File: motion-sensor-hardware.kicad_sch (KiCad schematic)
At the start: 34 parts, among them J1 MX128-2.54-04P-GN01-Cu-Y-A, J2 MX128-2.54-02P-GN01-Cu-Y-A, J4 Conn_01x02, J5 TYPE-C 16PIN 2MD(073), Q1 BSS138, SW1 SW_Push, SW2 SW_Push, U1 ESP32-C3-MINI-1-N4, U2 LD2410C, U5 ASSR-1218

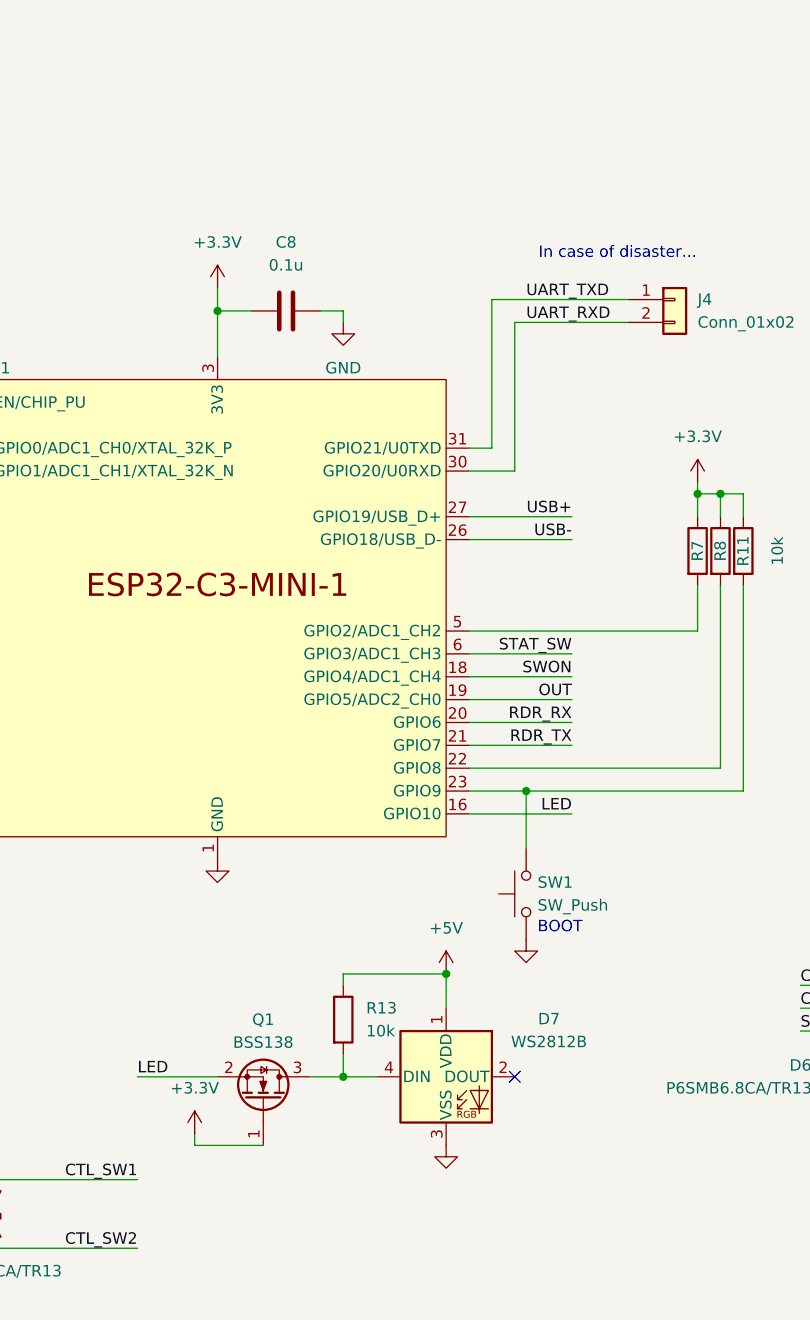
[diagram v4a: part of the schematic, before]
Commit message: Added decoupling cap for LED and bigger cap for module
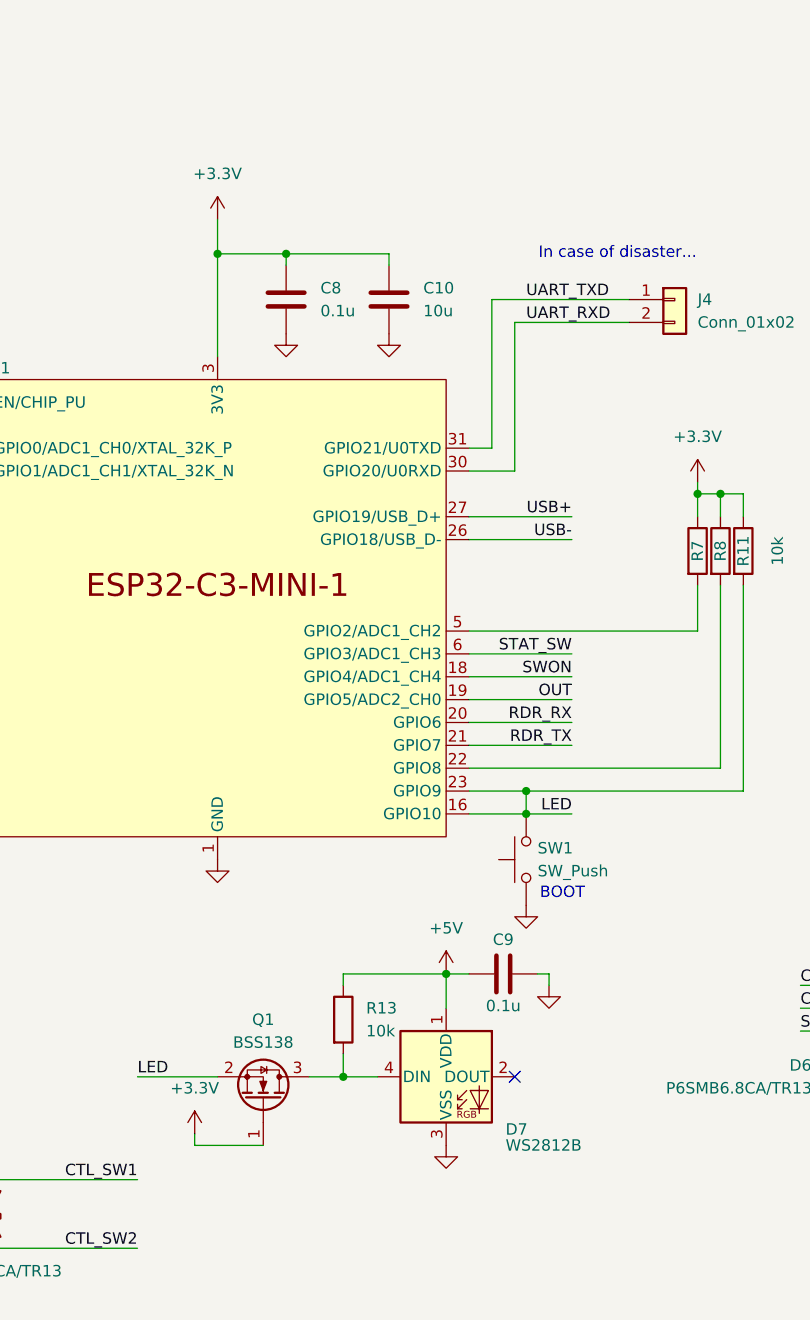
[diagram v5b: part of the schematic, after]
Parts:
- added C10: 10u, Capacitor_SMD:C_0805_2012Metric, symbol Device:C
- added C9: 0.1u, Capacitor_SMD:C_0805_2012Metric, symbol Device:C
- Q1: JLCPCB (none) -> C112239
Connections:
- net +3.3V: now also C8.2, C10.2; no longer C8.1
- net +5V: now also C9.2
- net GND: now also C8.1, C10.1, C9.1; no longer C8.2
- net LED: now also R11.2, SW1.2, U1.23 (GPIO9)
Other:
- moved on the sheet: C8, SW1

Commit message: Schematic relatively complete
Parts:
- removed C1: 0.1u, Capacitor_SMD:C_0805_2012Metric, symbol Device:C
- removed D3: LESD5D5.0CT1G, Diode_SMD:D_SOD-523, symbol Device:D_TVS
- removed D5: PTVS20VS1UR,115, Diode_SMD:Nexperia_DSN1608-2_1.6x0.8mm, symbol Diode:PTVS26VZ1USK
- removed J4: Conn_01x02, Connector_PinHeader_2.54mm:PinHeader_1x02_P2.54mm_Vertical, symbol Connector_Generic:Conn_01x02
- added D5: P6SMB24CA-E3/52, Diode_SMD:D_SMB, symbol Device:D_TVS
- added D8: BZT52C15S, Diode_SMD:D_SOD-323, symbol Device:D_Zener
- added F1: JK-nSMD100/16V, Fuse:Fuse_1206_3216Metric, symbol Device:Polyfuse
- added J3: PZ254V-11-03P, Connector_PinHeader_2.54mm:PinHeader_1x03_P2.54mm_Vertical, symbol Connector_Generic:Conn_01x03
- added Q2: XR30P10L, Package_TO_SOT_SMD:SOT-23, symbol Transistor_FET:Q_PMOS_GSD
- added R14: 100, Capacitor_SMD:C_0805_2012Metric, symbol Device:R
- added R15: 10k, Capacitor_SMD:C_0805_2012Metric, symbol Device:R
- D1, D2: JLCPCB C383211 -> C5199850
- R12: value 357Ω -> 330
- SW1, SW2: value SW_Push -> TS-1088-AR02016; footprint Button_Switch_SMD:SW_Push_1P1T_NO_CK_KMR2 -> Button_Switch_SMD:SW_Push_SPST_NO_Alps_SKRK; JLCPCB C221678 -> C720477
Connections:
- net GND: now also D5.1 (A1), J3.3 (Pin_3), R15.2
- net LED: no longer R11.2, SW1.2, U1.23 (GPIO9)
- net UART_RXD: now also J3.2 (Pin_2)
- net UART_TXD: now also J3.1 (Pin_1)
- net VIN: now also D8.1 (K), Q2.2 (S); no longer J2.1 (Pin_1)
- net VUSB: no longer names the net of J5.A4 (VBUS), J5.A9 (VBUS), J5.B4 (VBUS), J5.B9 (VBUS)
- new net: D8.2 (A), R14.2, R15.1
- new net: Q2.1 (G), R14.1
- new net: R11.2, SW1.2, U1.23 (GPIO9)
- new net: D5.2 (A2), F1.2, Q2.3 (D)
- new net VRAW: F1.1, J2.1 (Pin_1)
- no-connect marks 5 -> 6
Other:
- sheet Voltage Regulator ports: added V_{IN}; removed VIN
- moved on the sheet: J2
